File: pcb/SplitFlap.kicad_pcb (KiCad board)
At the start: 2 copper layers, 35 x 35 mm, 21 parts, among them J1 A1_3, U1 PCF8575DBR, U2 ULN2003

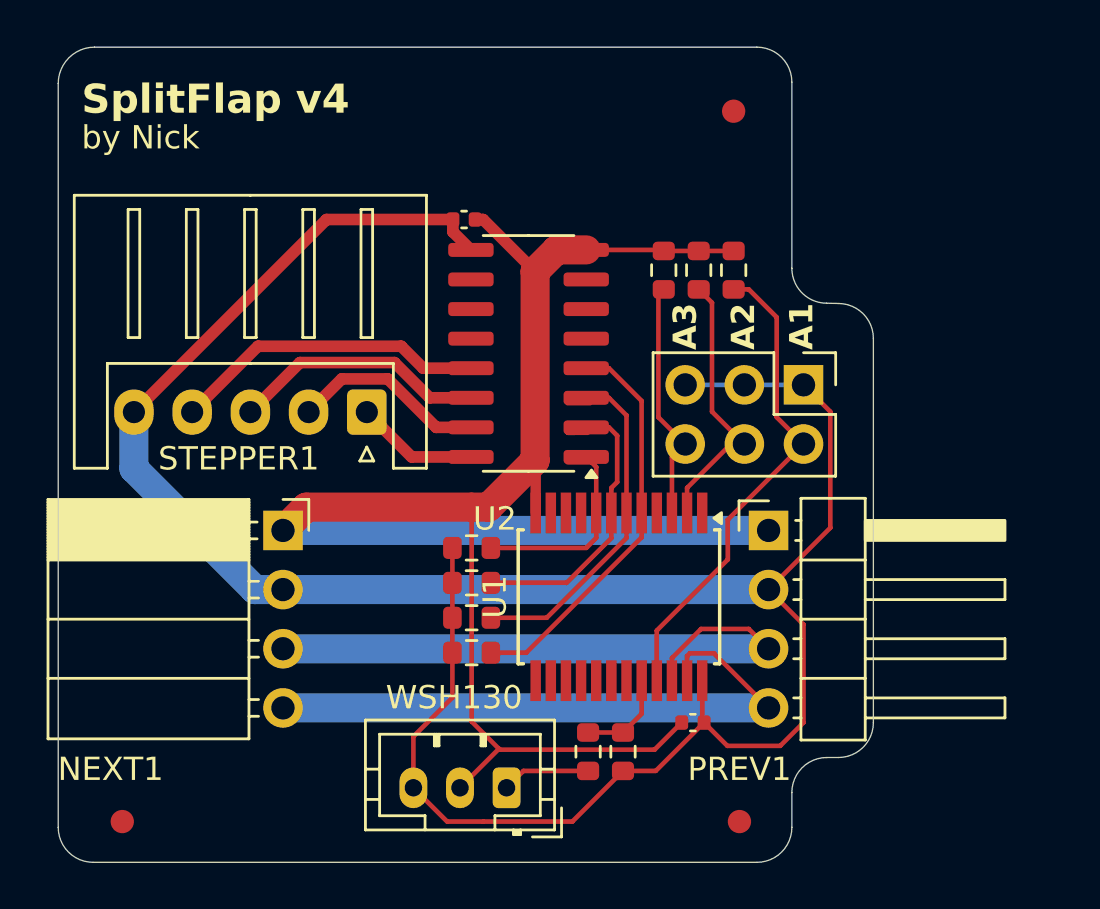
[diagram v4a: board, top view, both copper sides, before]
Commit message: Extend PCB to 37mm
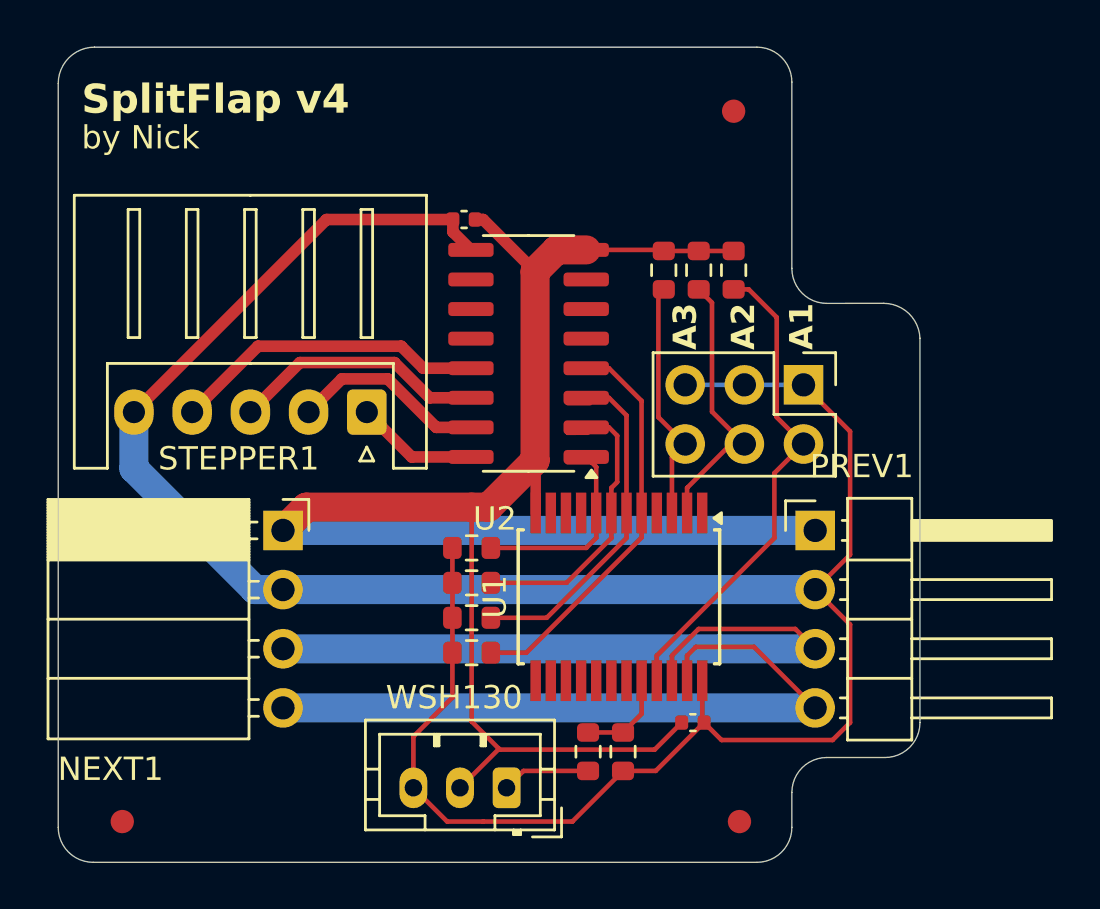
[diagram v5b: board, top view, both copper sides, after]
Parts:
- moved PREV1 2.00 mm to (177.5, 80.2)
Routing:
- net Net-(NEXT1-Pin_4): track 26.4 -> 30.7 mm
- net Net-(NEXT1-Pin_3): track 26.8 -> 30.9 mm
- net +5V: track 105.1 -> 108.8 mm
- net GND: track 77.8 -> 79.8 mm
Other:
- board size 35 x 35 mm -> 37 x 35 mm
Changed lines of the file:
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@@
 	(footprint "Connector_PinHeader_2.54mm:PinHeader_1x04_P2.54mm_Horizontal"
 		(layer "F.Cu")
-		(at 175.5 80.25)
+		(at 177.5 80.25)
 		(descr "Through hole angled pin header, 1x04, 2.54mm pitch, 6mm pin length, single row")
 		(tags "Through hole angled pin header THT 1x04 2.54mm single row")
 		(property "Reference" "PREV1"
-			(at -1.25 10.25 0)
+			(at 2 -2.75 0)
 			(layer "F.SilkS")
 			(effects
@@
 		)
 	)
-	(gr_line
-		(start 178.5 90)
-		(end 178 90)
-		(stroke
-			(width 0.05)
-			(type default)
-		)
-		(layer "Edge.Cuts")
-	)
 	(gr_arc
 		(start 176.5 91.5)
@@
 	)
 	(gr_arc
-		(start 180 88.5)
-		(mid 179.56066 89.56066)
-		(end 178.5 90)
+		(start 178.000057 70.501859)
+		(mid 176.939397 70.062519)
+		(end 176.500057 69.001859)
 		(stroke
 			(width 0.05)
@@
 		(layer "Edge.Cuts")
 	)
-	(gr_arc
-		(start 178 70.494462)
-		(mid 176.939348 70.055138)
-		(end 176.500041 68.994503)
-		(stroke
-			(width 0.05)
-			(type default)
-		)
-		(layer "Edge.Cuts")
-	)
 	(gr_line
 		(start 145 61.06066)
@@
 		(layer "Edge.Cuts")
 	)
+	(gr_arc
+		(start 180.43934 70.498822)
+		(mid 181.522067 70.935032)
+		(end 182 72)
+		(stroke
+			(width 0.05)
+			(type default)
+		)
+		(layer "Edge.Cuts")
+	)
 	(gr_line
 		(start 176.500057 69.001859)
@@
 	)
 	(gr_line
-		(start 178.5 70.505497)
-		(end 178 70.494503)
+		(start 178 90)
+		(end 180.5 90)
 		(stroke
 			(width 0.05)
@@
 	)
 	(gr_line
-		(start 180 72.0055)
-		(end 180 88.5)
+		(start 182 72)
+		(end 182 88.4945)
 		(stroke
 			(width 0.05)
@@
 	)
 	(gr_arc
-		(start 178.5 70.505497)
-		(mid 179.560641 70.94484)
-		(end 180 72.005497)
+		(start 182 88.5)
+		(mid 181.56066 89.56066)
+		(end 180.5 90)
+		(stroke
+			(width 0.05)
+			(type default)
+		)
+		(layer "Edge.Cuts")
+	)
+	(gr_line
+		(start 180.43934 70.498823)
+		(end 178.0001 70.501859)
 		(stroke
 			(width 0.05)
@@
 	)
 	(gr_text "GND"
-		(at 179.75 80.219 0)
+		(at 181.75 80.219 0)
 		(layer "B.SilkS")
 		(effects
@@
 	)
 	(gr_text "SDA"
-		(at 179.75 86.469 0)
+		(at 181.75 86.469 0)
 		(layer "B.SilkS")
 		(effects
@@
 	)
 	(gr_text "SCL"
-		(at 179.75 84.469 0)
+		(at 181.75 84.469 0)
 		(layer "B.SilkS")
 		(effects
@@
 	)
 	(gr_text "+5V"
-		(at 180 82.469 0)
+		(at 182 82.469 0)
 		(layer "B.SilkS")
 		(effects
@@
 	)
 	(segment
-		(start 177 74)
-		(end 178.151 75.151)
-		(width 0.2)
-		(layer "F.Cu")
-		(net 1)
-	)
-	(segment
 		(start 161.925 84)
 		(end 161.925 82.5)
@@
 	)
 	(segment
+		(start 179 88.5)
+		(end 178.25 89.25)
+		(width 0.2)
+		(layer "F.Cu")
+		(net 1)
+	)
+	(segment
+		(start 179 76)
+		(end 177 74)
+		(width 0.2)
+		(layer "F.Cu")
+		(net 1)
+	)
+	(segment
+		(start 173.48 89.25)
+		(end 172.73 88.5)
+		(width 0.2)
+		(layer "F.Cu")
+		(net 1)
+	)
+	(segment
+		(start 177.5 82.79)
+		(end 179 81.29)
+		(width 0.2)
+		(layer "F.Cu")
+		(net 1)
+	)
+	(segment
 		(start 161.7 92.75)
 		(end 160.25 91.3)
@@
 	)
 	(segment
-		(start 177 84.29)
-		(end 177 88.5)
-		(width 0.2)
-		(layer "F.Cu")
-		(net 1)
-	)
-	(segment
-		(start 175.5 82.79)
-		(end 177 84.29)
+		(start 178.25 89.25)
+		(end 173.48 89.25)
 		(width 0.2)
 		(layer "F.Cu")
@@
 	)
 	(segment
-		(start 177 88.5)
-		(end 176 89.5)
-		(width 0.2)
-		(layer "F.Cu")
-		(net 1)
-	)
-	(segment
-		(start 178.151 75.151)
-		(end 178.151 80.139)
+		(start 179 81.29)
+		(end 179 76)
 		(width 0.2)
 		(layer "F.Cu")
@@
 	)
 	(segment
-		(start 178.151 80.139)
-		(end 175.5 82.79)
-		(width 0.2)
-		(layer "F.Cu")
-		(net 1)
-	)
-	(segment
 		(start 160.25 89.1)
 		(end 160.25 91.3)
@@
 	)
 	(segment
-		(start 173.73 89.5)
-		(end 172.73 88.5)
-		(width 0.2)
-		(layer "F.Cu")
-		(net 1)
-	)
-	(segment
 		(start 161.945 66.9)
 		(end 161.945 67.43)
@@
 	)
 	(segment
+		(start 179 84.29)
+		(end 179 88.5)
+		(width 0.2)
+		(layer "F.Cu")
+		(net 1)
+	)
+	(segment
 		(start 161.945 67.43)
 		(end 162.72 68.205)
@@
 	)
 	(segment
-		(start 176 89.5)
-		(end 173.73 89.5)
+		(start 177.5 82.79)
+		(end 179 84.29)
 		(width 0.2)
 		(layer "F.Cu")
@@
 	)
 	(segment
+		(start 177.5 82.79)
+		(end 154.65 82.79)
+		(width 1.25)
+		(layer "B.Cu")
+		(net 1)
+	)
+	(segment
 		(start 148.25 77.592081)
 		(end 148.25 75.169)
@@
 	)
 	(segment
-		(start 154.65 82.79)
-		(end 175.5 82.79)
-		(width 1.25)
-		(layer "B.Cu")
-		(net 1)
-	)
-	(segment
 		(start 177 74)
 		(end 174.46 74)
@@
 	)
 	(segment
-		(start 175.5 80.25)
-		(end 154.65 80.25)
+		(start 154.65 80.25)
+		(end 177.5 80.25)
 		(width 1.25)
 		(layer "B.Cu")
@@
 	)
 	(segment
-		(start 171.35 85.7309)
-		(end 172.6009 84.48)
+		(start 172.495 84.48)
+		(end 171.35 85.625)
 		(width 0.2)
 		(layer "F.Cu")
@@
 	)
 	(segment
-		(start 171.35 86.7)
-		(end 171.35 85.7309)
+		(start 176.65 84.48)
+		(end 172.495 84.48)
 		(width 0.2)
 		(layer "F.Cu")
@@
 	)
 	(segment
-		(start 172.6009 84.48)
-		(end 174.65 84.48)
+		(start 177.5 85.33)
+		(end 176.65 84.48)
 		(width 0.2)
 		(layer "F.Cu")
@@
 	)
 	(segment
-		(start 174.65 84.48)
-		(end 175.5 85.33)
+		(start 171.35 85.625)
+		(end 171.35 86.7)
 		(width 0.2)
 		(layer "F.Cu")
@@
 	)
 	(segment
-		(start 175.5 85.33)
-		(end 154.65 85.33)
+		(start 154.65 85.33)
+		(end 177.5 85.33)
 		(width 1.25)
 		(layer "B.Cu")
@@
 	(segment
 		(start 172 86.7)
-		(end 172 85.648)
+		(end 172 85.625)
 		(width 0.2)
 		(layer "F.Cu")
@@
 	)
 	(segment
-		(start 173.154 85.524)
-		(end 175.5 87.87)
+		(start 172 85.625)
+		(end 172.375 85.25)
 		(width 0.2)
 		(layer "F.Cu")
@@
 	)
 	(segment
-		(start 172.124 85.524)
-		(end 173.154 85.524)
+		(start 172.375 85.25)
+		(end 174.88 85.25)
 		(width 0.2)
 		(layer "F.Cu")
@@
 	)
 	(segment
-		(start 172 85.648)
-		(end 172.124 85.524)
+		(start 174.88 85.25)
+		(end 177.5 87.87)
 		(width 0.2)
 		(layer "F.Cu")
@@
 	)
 	(segment
-		(start 154.65 87.87)
-		(end 175.5 87.87)
+		(start 177.5 87.87)
+		(end 154.65 87.87)
 		(width 1.25)
 		(layer "B.Cu")
@@
 	)
 	(segment
-		(start 173.75 79.79)
-		(end 173.75 81.5)
+		(start 177 76.54)
+		(end 175.75 77.79)
 		(width 0.2)
 		(layer "F.Cu")
@@
 	)
 	(segment
-		(start 173.75 81.5)
-		(end 170.7 84.55)
+		(start 175.75 77.79)
+		(end 175.75 80.575)
 		(width 0.2)
 		(layer "F.Cu")
@@
 	)
 	(segment
-		(start 177 76.54)
-		(end 173.75 79.79)
-		(width 0.2)
-		(layer "F.Cu")
-		(net 34)
-	)
-	(segment
-		(start 170.7 84.55)
-		(end 170.7 86.7)
+		(start 175.75 80.575)
+		(end 170.7 85.625)
 		(width 0.2)
 		(layer "F.Cu")
@@
 		(start 175.849 71.099)
 		(end 175.849 75.389)
+		(width 0.2)
+		(layer "F.Cu")
+		(net 34)
+	)
+	(segment
+		(start 170.7 85.625)
+		(end 170.7 86.7)
 		(width 0.2)
 		(layer "F.Cu")
@@
 		)
 	)
-	(group ""
-		(members "58991a2b-1f7d-4756-97ff-3d6ca5b602cb" "a6e3d66e-2c96-4dec-b52b-d89cb1ee3174"
-			"df1a40b3-adb2-402d-8ad8-8a3584952633"
-		)
-	)

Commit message: Bump printed version number
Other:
- board text added: "SplitFlap v5"
- board text removed: "SplitFlap v4"
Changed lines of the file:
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@@
 		)
 	)
-	(gr_text "SplitFlap v4"
+	(gr_text "SplitFlap v5"
 		(at 146 62.469 0)
 		(layer "F.SilkS")
